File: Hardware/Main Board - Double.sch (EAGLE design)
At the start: 77 parts, among them J1 MICROMOD-2222-C, J10 MICRO-SD-PUSH-PUSH-EXT-PIN, J2 Vertical Qwiic Connector, J4 QWIIC_RIGHT_ANGLE, J5 CORTEX_JTAG_DEBUG_MINIMUM_PTH, J6 MICROMOD_FUNCTION_MAIN, J7 MICROMOD_FUNCTION_MAIN, Q1 3.1A/30V/105mΩ, U1 STG3856QTR, U2 MCP73831, U5 AP7361C-33

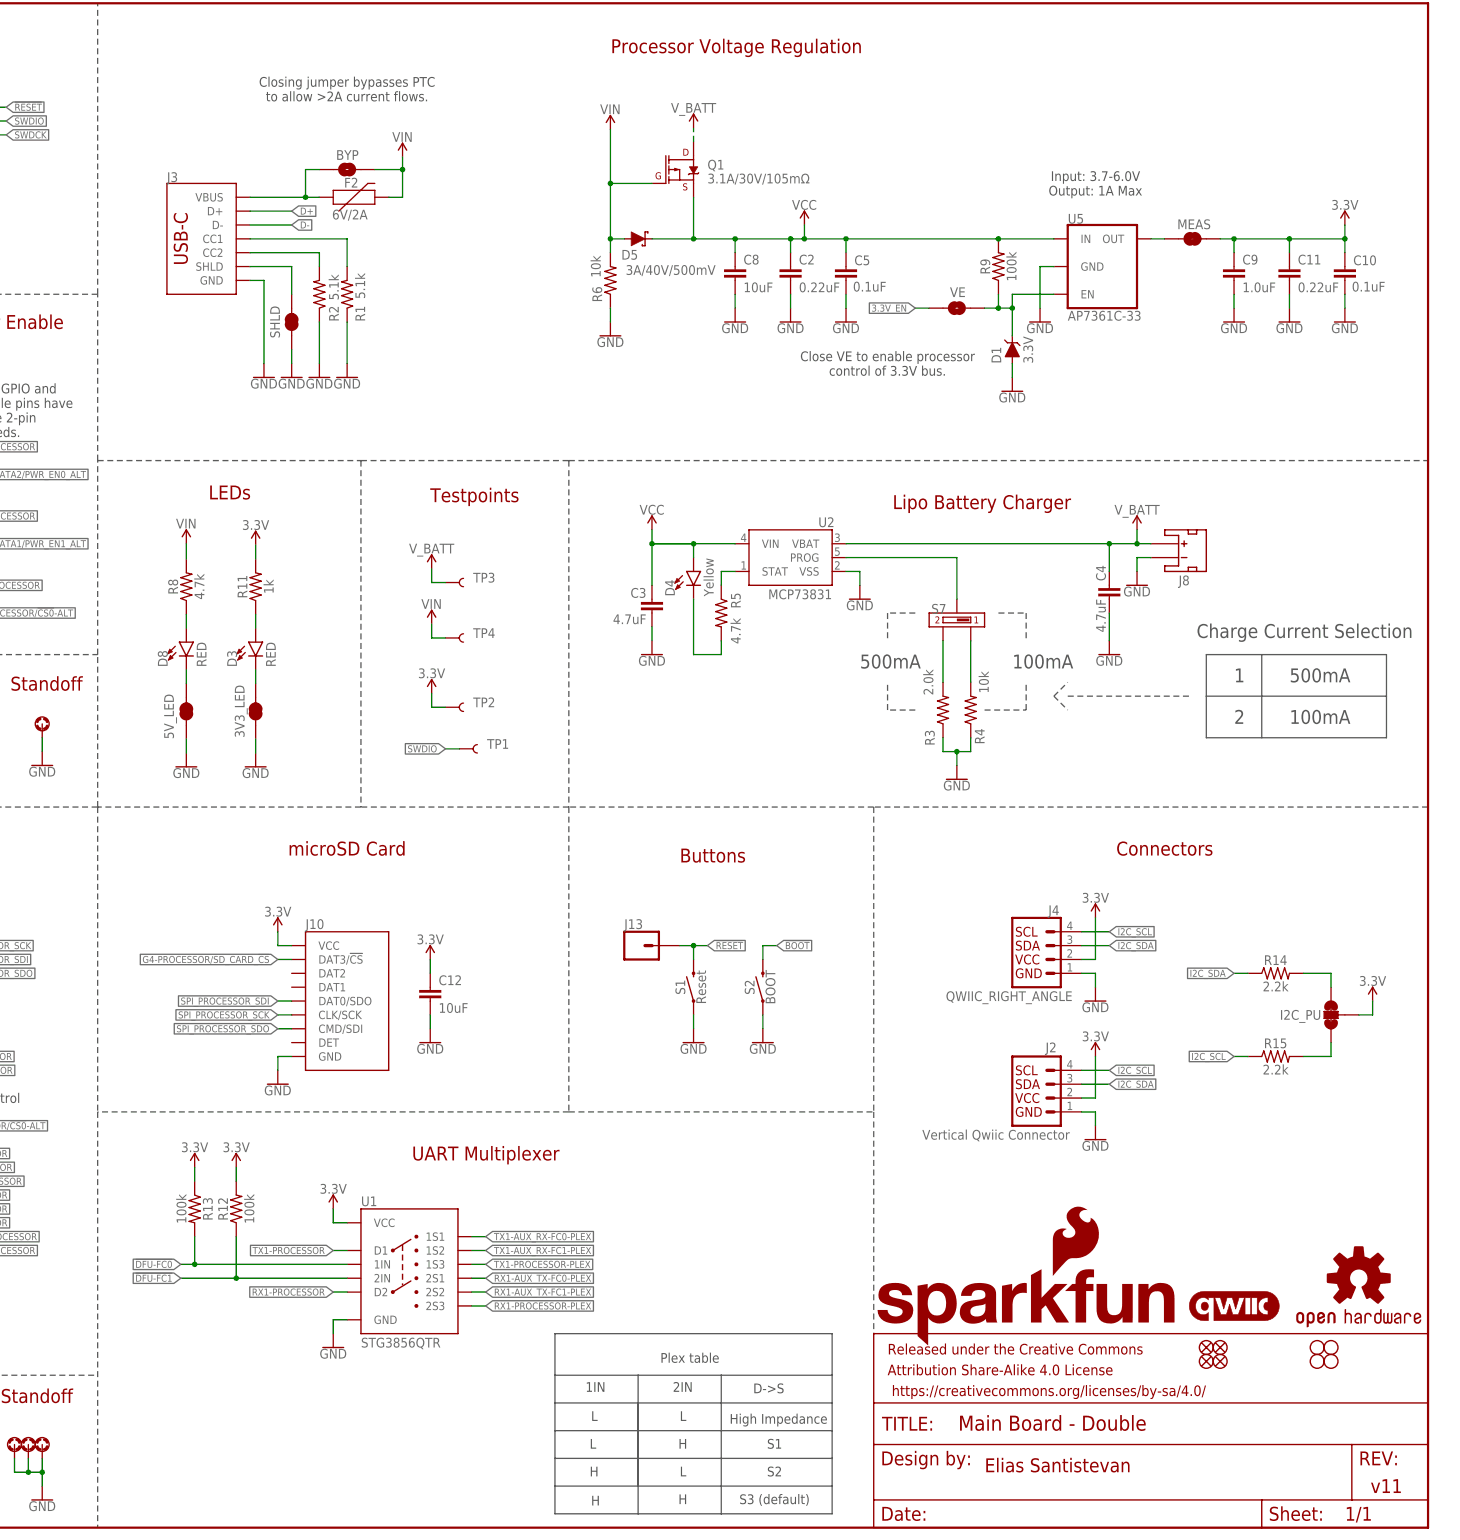
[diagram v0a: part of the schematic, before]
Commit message: Fixes ground pour in areas throughout, adds vias, updates net positioning and text layout in schematic
* Increases cap on output of VREG
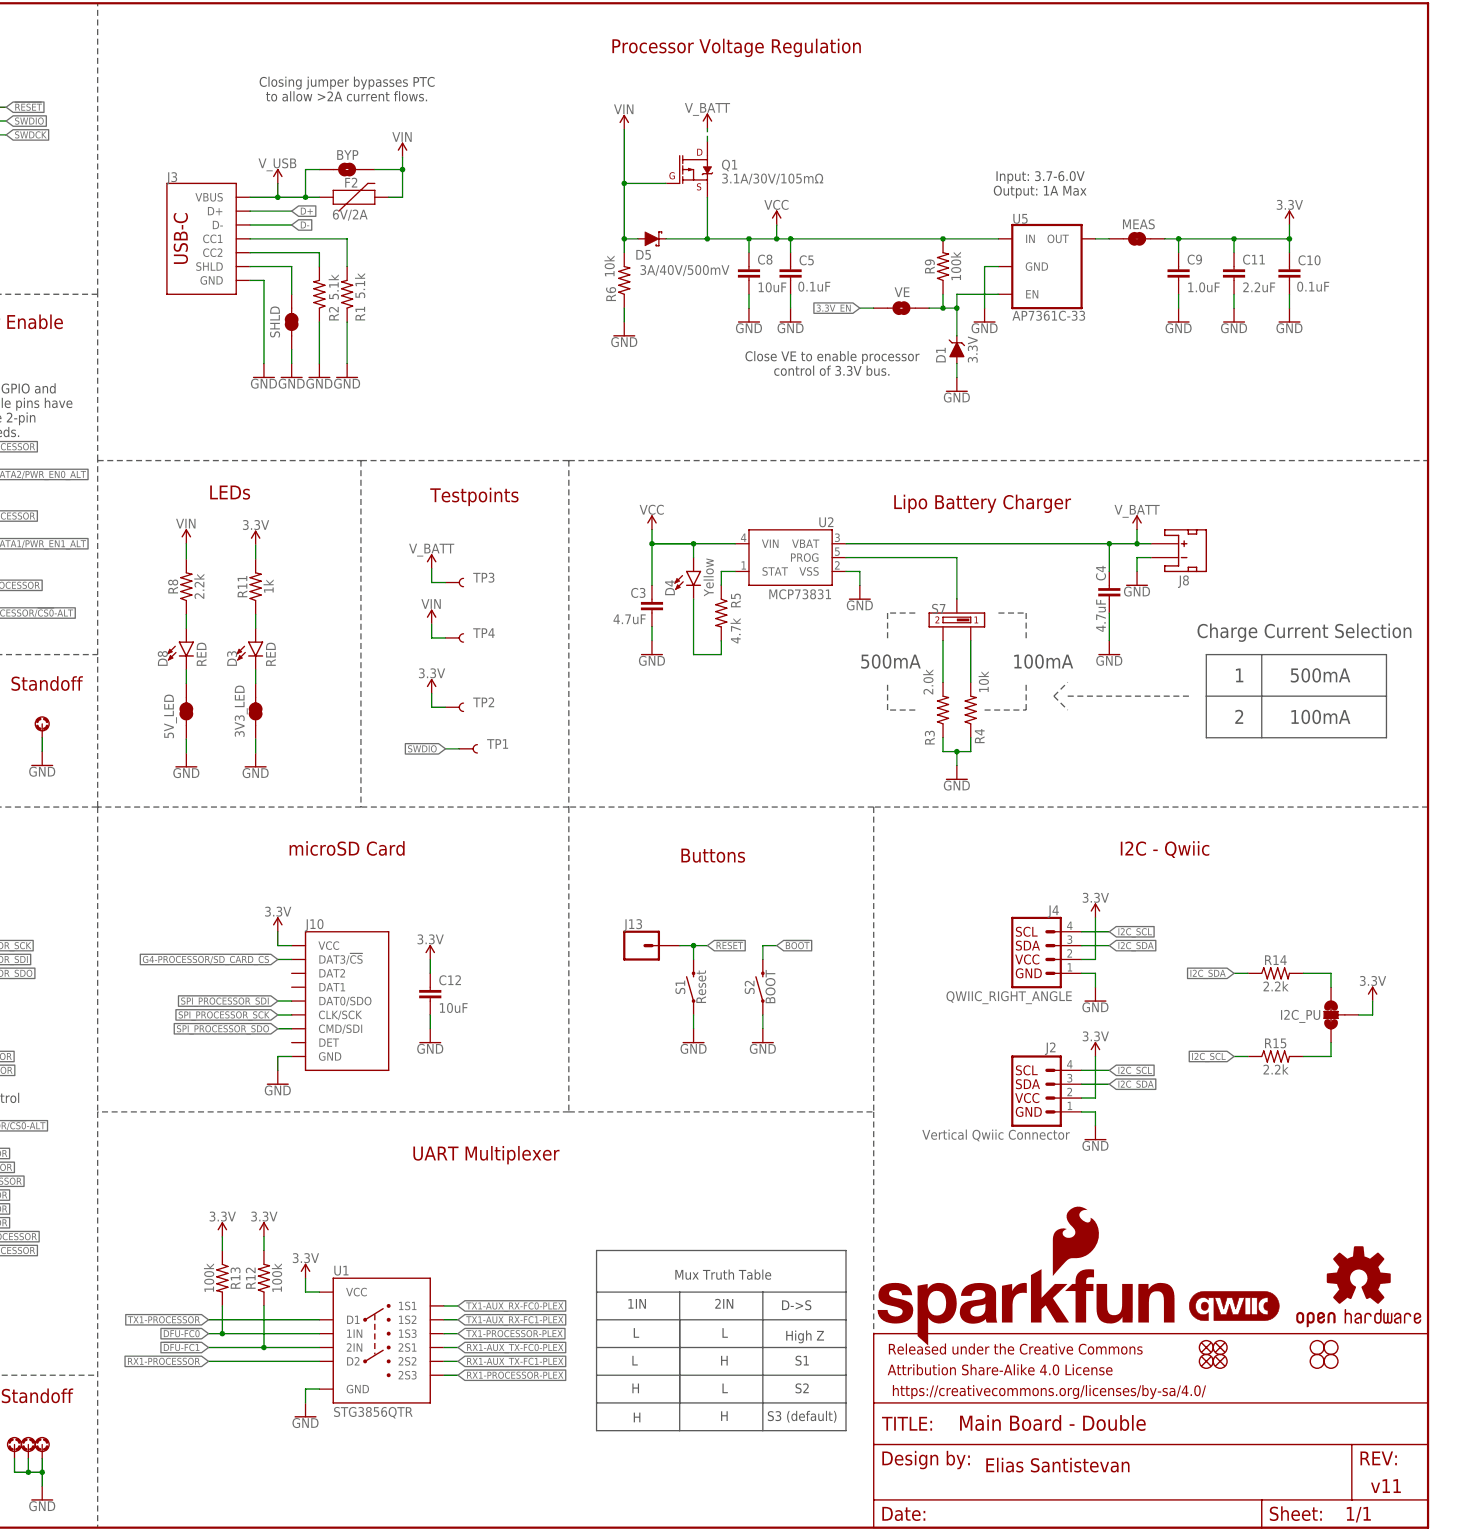
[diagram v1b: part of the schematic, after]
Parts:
- removed C2: 0.22uF, SparkFun-Capacitors:0.22UF-0603-25V-10%
- C11: value 0.22uF -> 2.2uF; device SparkFun-Capacitors:0.22UF-0603-25V-10% -> SparkFun-Capacitors:2.2UF-0603-10V-20%
- R8: value 4.7k -> 2.2k; device SparkFun-Resistors:4.7KOHM-0603-1/10W-1% -> SparkFun-Resistors:2.2KOHM-0603-1/10W-1%
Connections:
- net N$7 renamed V_USB
- net GND: no longer C2.2
- net VCC: no longer C2.1
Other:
- note added: "High Z"
- note added: "I2C - Qwiic"
- note added: "Mux Truth Table"
- note removed: "Connectors"
- note removed: "High Impedance"
- note removed: "Plex table"
- moved on the sheet: C10, C11, C5, C8, C9, D1, D5, MEAS, Q1, R12, R13, R6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

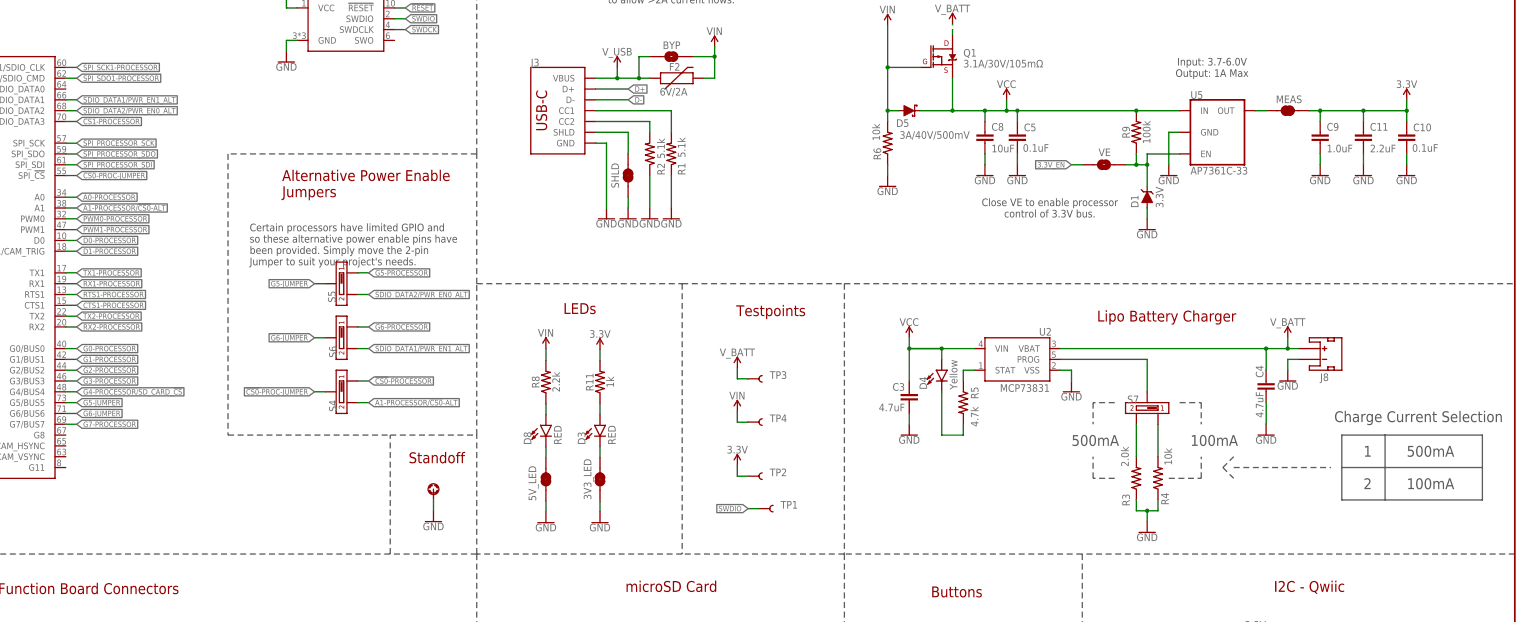
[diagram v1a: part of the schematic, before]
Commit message: Improves routing, snaps many parts to a much more sensible grid, removes some caps on INPUT and OUTPUT of VREG that were not necessary
* Adds another MEAS Jumper for 5V side
* Removes selection on charge circuit (500mA now only)
* Fixes chip select not being double routed corectly
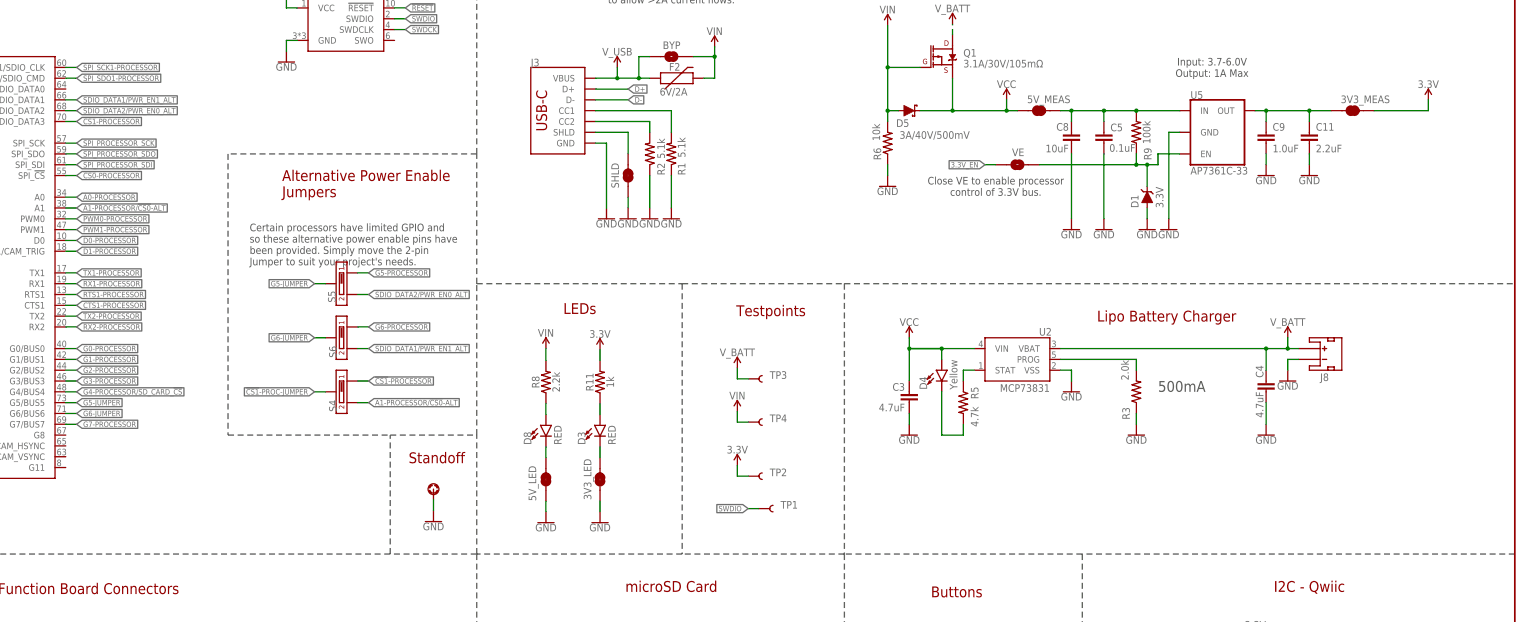
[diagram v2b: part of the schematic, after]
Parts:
- removed C10: 0.1uF, SparkFun-Capacitors:0.1UF-0603-25V-(+80/-20%)
- removed MEAS: JUMPER-COMBO_2_NC_TRACE, SparkFun-Jumpers:JUMPER-COMBO_2_NC_TRACE
- removed R4: 10k, SparkFun-Resistors:10KOHM-0603-1/10W-1%
- removed S7: DIPSWITCH-3-PIN, dip_switch:DIPSWITCH-3-PIN
- added 3V3_MEAS, 5V_MEAS: JUMPER-COMBO_2_NC_TRACE, SparkFun-Jumpers:JUMPER-COMBO_2_NC_TRACE
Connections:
- removed net !CS0!-PROC-JUMPER: J1.SPI_!CS!, S4.2
- removed net N$8: R3.2, S7.1
- removed net N$9: R4.2, S7.3
- new net !CS1!-PROC-JUMPER: S4.2
- new net VCC_MEAS: 5V_MEAS.2, C5.1, C8.1, R9.2, U5.IN
- net !CS0!-PROCESSOR: now also J1.SPI_!CS!; no longer S4.3
- net !CS1!-PROCESSOR: now also S4.3
- net 3.3V: now also 3V3_MEAS.2; no longer C10.1, C11.1, C9.1, MEAS.2
- net GND: no longer C10.2, R4.1
- net N$1: now also 3V3_MEAS.1, C11.1, C9.1; no longer MEAS.1
- net N$6: now also R3.2; no longer S7.2
- net VCC: now also 5V_MEAS.1; no longer C5.1, C8.1, R9.2, U5.IN
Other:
- note removed: "1"
- note removed: "100mA"
- note removed: "2"
- note removed: "Charge Current Selection"
- moved on the sheet: C11, C5, C8, C9, R3, VE

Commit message: Many more grid improvements
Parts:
- added J9: (no value), SparkFun-Connectors:CONN_01PTH_NO_SILK_YES_STOP
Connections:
- net GND: now also J9.1
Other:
- moved on the sheet: C3, C4, D4, J8, R3, R5, U2
